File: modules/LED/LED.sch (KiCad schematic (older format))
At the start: 49 parts, among them J1 2, J10 11, J11 12, J12 13, J13 A0, J14 A1, J15 A2, J16 A3, J17 A4, J18 A5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

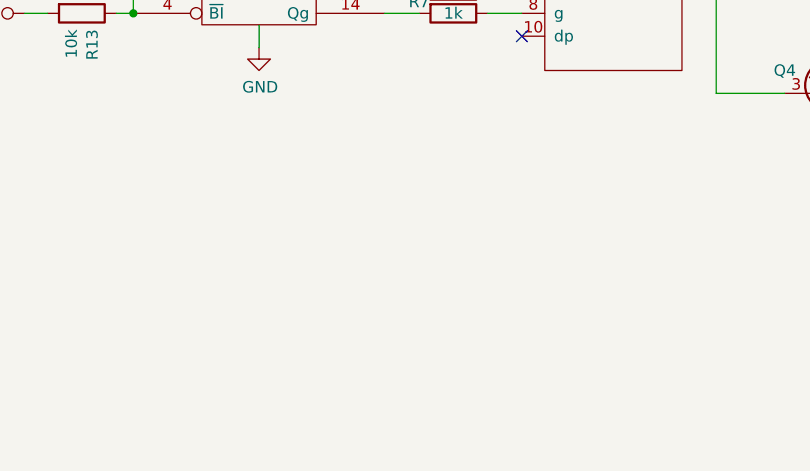
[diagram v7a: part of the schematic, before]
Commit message: Pull-up 74HS139
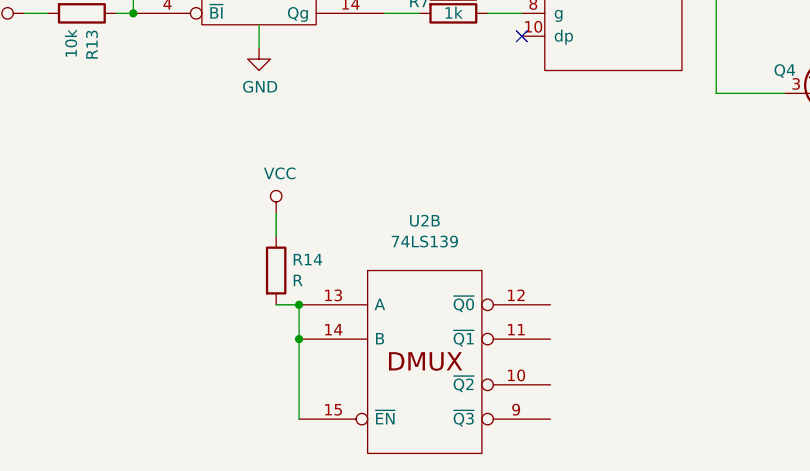
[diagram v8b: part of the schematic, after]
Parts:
- added R14: R, Resistor_SMD:R_0805_2012Metric_Pad1.15x1.40mm_HandSolder, symbol Device:R
- added unit 2 of U2
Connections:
- wire segments 112 -> 116
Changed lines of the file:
@@
 NoConn ~ 1200 3550
 $Comp
-L power:GND #PWR?
+L power:GND #PWR0105
 U 1 1 5D8A7568
 P 2800 3150
-F 0 "#PWR?" H 2800 2900 50  0001 C CNN
+F 0 "#PWR0105" H 2800 2900 50  0001 C CNN
 F 1 "GND" H 2805 2977 50  0000 C CNN
 F 2 "" H 2800 3150 50  0001 C CNN
@@
 	2800 3050 2800 3150
 $Comp
-L power:VCC #PWR?
+L power:VCC #PWR0106
 U 1 1 5D9A7B3F
 P 5575 5100
-F 0 "#PWR?" H 5575 4950 50  0001 C CNN
+F 0 "#PWR0106" H 5575 4950 50  0001 C CNN
 F 1 "VCC" V 5592 5228 50  0000 L CNN
 F 2 "" H 5575 5100 50  0001 C CNN
@@
 	5300 5100 5575 5100
 Connection ~ 5300 5100
+$Comp
+L Device:R R14
+U 1 1 5D9BDDF0
+P 2675 5875
+F 0 "R14" H 2745 5921 50  0000 L CNN
+F 1 "R" H 2745 5830 50  0000 L CNN
+F 2 "Resistor_SMD:R_0805_2012Metric_Pad1.15x1.40mm_HandSolder" V 2605 5875 50  0001 C CNN
+F 3 "~" H 2675 5875 50  0001 C CNN
+	1    2675 5875
+	1    0    0    -1
+$EndComp
+$Comp
+L power:VCC #PWR0107
+U 1 1 5D9BEFB1
+P 2675 5625
+F 0 "#PWR0107" H 2675 5475 50  0001 C CNN
+F 1 "VCC" H 2692 5798 50  0000 C CNN
+F 2 "" H 2675 5625 50  0001 C CNN
+F 3 "" H 2675 5625 50  0001 C CNN
+	1    2675 5625
+	1    0    0    -1
+$EndComp
+Wire Wire Line
+	2675 5625 2675 5725
+Wire Wire Line
+	2675 6025 2775 6025
+Wire Wire Line
+	2775 6025 2775 6175
+$Comp
+L 74xx_IEEE:74LS139 U2
+U 2 1 5D9D9597
+P 3325 6275
+F 0 "U2" H 3325 6891 50  0000 C CNN
+F 1 "74LS139" H 3325 6800 50  0000 C CNN
+F 2 "Package_SO:SOIC-16_3.9x9.9mm_P1.27mm" H 3325 6275 50  0001 C CNN
+F 3 "" H 3325 6275 50  0001 C CNN
+	2    3325 6275
+	1    0    0    -1
+$EndComp
+Connection ~ 2775 6025
+Wire Wire Line
+	2775 6525 2775 6175
+Connection ~ 2775 6175
 $EndSCHEMATC
